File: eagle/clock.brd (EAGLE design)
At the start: 160 x 100 mm, 55 parts, among them CN1 ARDUINO_SHIELDNO_SILK, IC1 TPS55330TRE, IC2 TCS3472FN, Q1 BC817-40SMD, Q2 SUD50P04-13L

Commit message: came up with a better location for the buttons
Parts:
- moved LED0 101.0 mm to (14.0, 69.0)
- moved LED6 100.3 mm to (14.0, 57.0)
- moved LED12 99.7 mm to (14.0, 45.0)
- moved LED1 97.1 mm to (26.0, 69.0)
- moved LED7 96.3 mm to (26.0, 57.0)
- moved LED13 95.8 mm to (26.0, 45.0)
- moved LED2 93.2 mm to (38.0, 69.0)
- moved LED8 92.4 mm to (38.0, 57.0)
- moved LED14 91.8 mm to (38.0, 45.0)
- moved LED3 89.3 mm to (50.0, 69.0)
- moved LED9 88.5 mm to (50.0, 57.0)
- moved LED15 87.8 mm to (50.0, 45.0)
- moved LED4 85.4 mm to (62.0, 69.0)
- moved LED10 84.5 mm to (62.0, 57.0)
- moved LED16 83.9 mm to (62.0, 45.0)
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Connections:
- removed net N$26: CN1.A0, LEFT.P$1
- removed net N$27: CN1.A1, DOWN.P$1
- removed net N$28: CN1.A2, UP.P$1
- removed net N$29: CN1.A3, RIGHT.P$1
- new net N$1: CN1.A3, LEFT.P$1
- new net N$2: CN1.A2, DOWN.P$1
- new net N$3: CN1.A1, UP.P$1
- new net N$4: CN1.A0, RIGHT.P$1

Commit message: Almost finished layout
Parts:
- added C19: 10uF, rcl:C1206K
- added R9: 1k, rcl:R0603
- moved R5 105.6 mm to (64.8, 5.08), flipped to the bottom
- moved Q1 101.1 mm to (70.5, 3.17), flipped to the bottom, turned to 180 degrees
- moved R6 89.9 mm to (73.7, 5.08), flipped to the bottom, turned to 270 degrees
- moved Q2 89.9 mm to (80.6, 5.08), flipped to the bottom, turned to 90 degrees
- moved R7 84.9 mm to (16.5, 48.9), turned to 0 degrees
- moved R8 82.5 mm to (16.5, 50.8), turned to 0 degrees
- moved IC2 81.5 mm to (18.2, 50.8), turned to 270 degrees
- moved C10 80.2 mm to (16.5, 52.7), turned to 0 degrees
- moved C18 79.9 mm to (14.0, 46.4)
- moved C7 75.5 mm to (81.9, 34.9), flipped to the bottom, turned to 180 degrees
- moved C8 72.1 mm to (81.9, 37.5), flipped to the bottom, turned to 180 degrees
- moved D1 70.5 mm to (76.2, 38.7), flipped to the bottom, turned to 90 degrees
- moved L1 70.5 mm to (67.3, 38.7), flipped to the bottom, turned to 180 degrees
- moved C13 70.5 mm to (64.8, 15.9), turned to 90 degrees
- moved C9 69.0 mm to (81.9, 40.0), flipped to the bottom, turned to 180 degrees
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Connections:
- new net N$6: CN1.TX, R9.1
- net GND: now also C19.2
- net LIGHT-INT: now also R9.2; no longer CN1.D7
- net PWR-EN: now also CN1.A5; no longer CN1.D9
- net SMPSU-OUTPUT: now also C19.1
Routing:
- net 3.3V: track 9.12 -> 282.4 mm, vias 1 -> 19
- net 5V: track 0.00 -> 271.1 mm, vias 0 -> 24
- net N$25: track 0.00 -> 80.0 mm, vias 0 -> 2
- net N$19: track 0.00 -> 77.3 mm
- net LED-DATA: track 0.00 -> 75.9 mm
- net N$6: track 0.00 -> 74.4 mm, vias 0 -> 1
- net SCL: track 2.36 -> 76.3 mm
- net SDA: track 3.16 -> 68.6 mm
- net SMPSU-OUTPUT: track 16.5 -> 67.8 mm
- net PWR-EN: track 0.00 -> 50.0 mm
- net N$4: track 0.00 -> 43.9 mm
- net SW: track 0.00 -> 31.2 mm
- net N$3: track 0.00 -> 28.6 mm
- net LED-PWM: track 0.00 -> 26.9 mm
- net N$1: track 0.00 -> 18.9 mm
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- added copper zone on layer 1, net GND
- added copper zone on layer 16, net GND
- removed copper zone on layer 1, net SMPSU-OUTPUT
- removed copper zone on layer 1, net SW
- removed copper zone on layer 1, net V_BATT
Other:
- board size 160 x 100 mm -> 78.7 x 78.7 mm

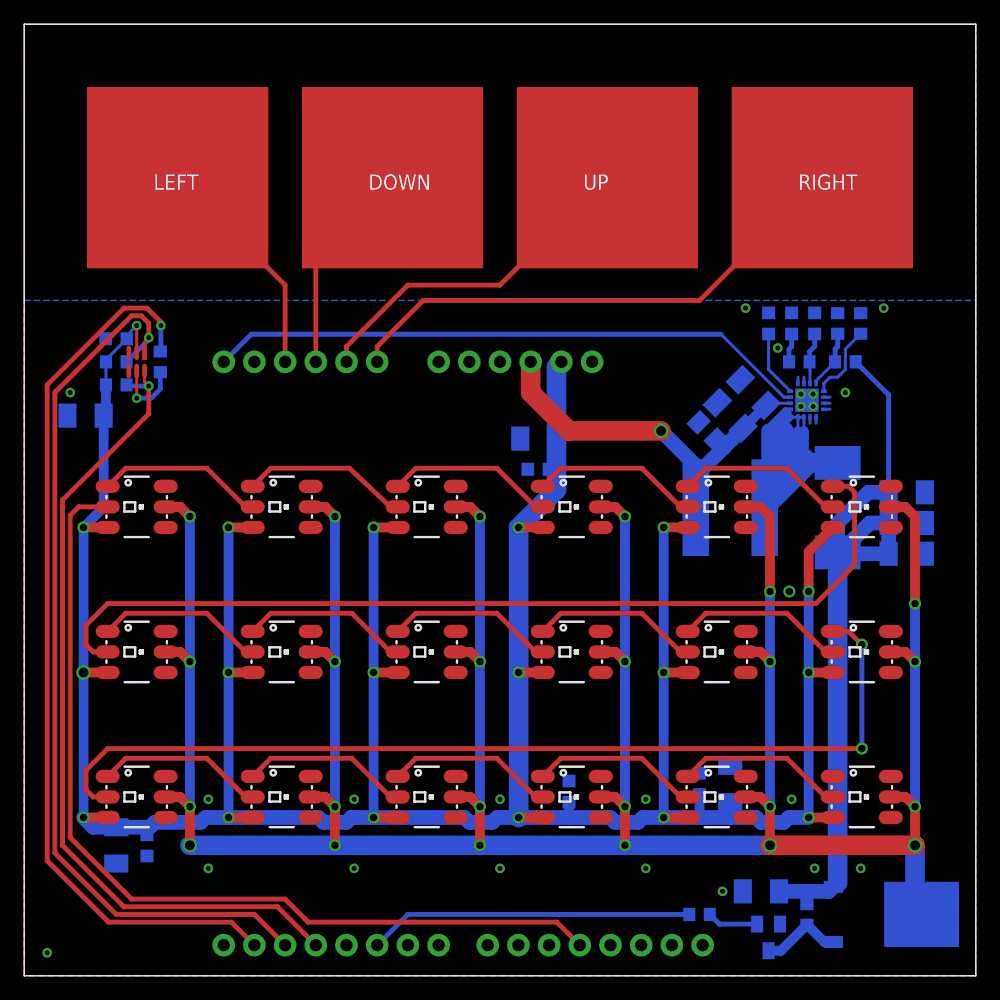
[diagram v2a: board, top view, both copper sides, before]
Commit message: Seems like there's a bug with the polyfills in eagle. I gave up and I just used one back plane
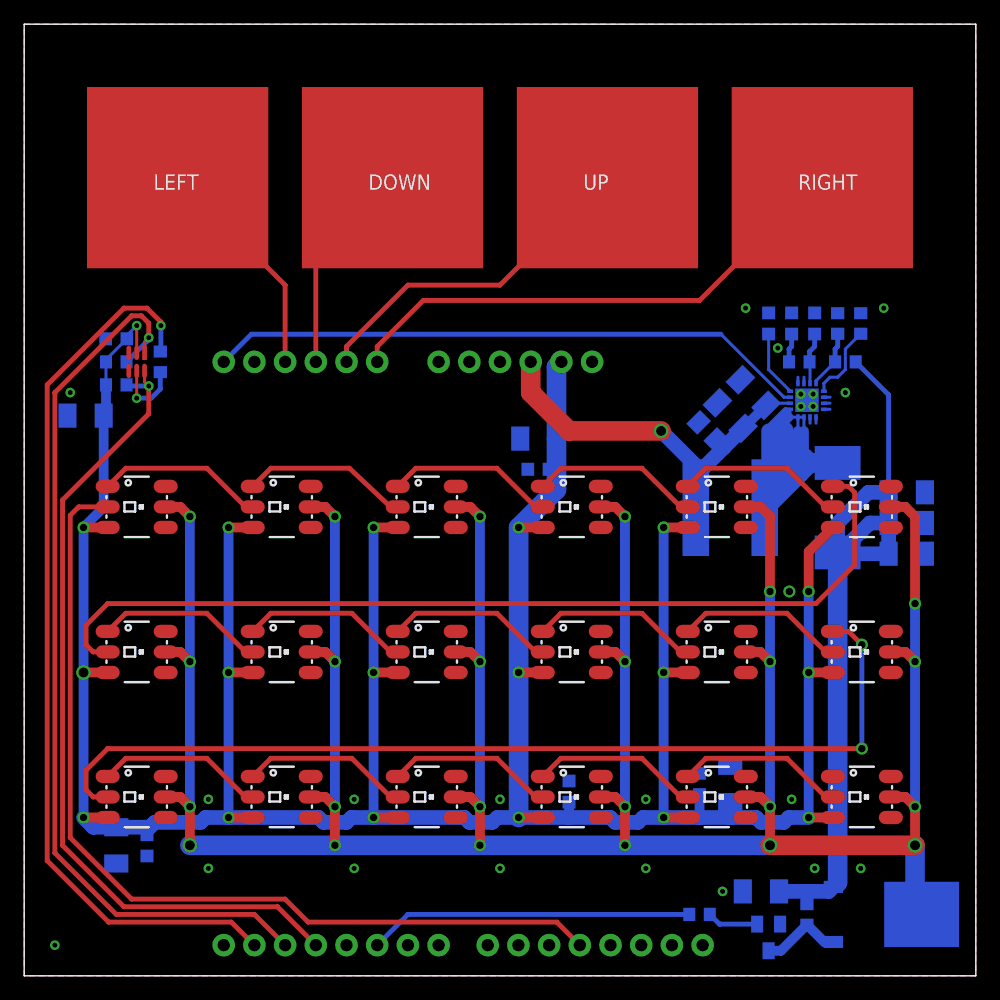
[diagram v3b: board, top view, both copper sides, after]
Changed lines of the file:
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@@
 <grid distance="25" unitdist="mil" unit="mil" style="dots" multiple="1" display="yes" altdistance="0.025" altunitdist="inch" altunit="inch"/>
 <layers>
-<layer number="1" name="Top" color="4" fill="1" visible="yes" active="yes"/>
+<layer number="1" name="Top" color="4" fill="1" visible="no" active="yes"/>
 <layer number="2" name="Route2" color="1" fill="3" visible="no" active="no"/>
 <layer number="3" name="Route3" color="4" fill="3" visible="no" active="no"/>
@@
 <contactref element="LED17" pad="6"/>
 <contactref element="C19" pad="2"/>
-<polygon width="0.254" layer="16" isolate="0.254">
-<vertex x="8.89" y="55.88"/>
-<vertex x="87.63" y="55.88"/>
+<polygon width="0.254" layer="16" pour="hatch" isolate="0.254">
+<vertex x="8.89" y="78.74"/>
+<vertex x="87.63" y="78.74"/>
 <vertex x="87.63" y="0"/>
 <vertex x="8.89" y="0"/>
@@
 <via x="36.195" y="8.89" extent="1-16" drill="0.4064" diameter="0.4064" shape="octagon"/>
 <via x="24.13" y="8.89" extent="1-16" drill="0.4064" diameter="0.4064" shape="octagon"/>
-<via x="10.795" y="1.905" extent="1-16" drill="0.4064" diameter="0.4064" shape="octagon"/>
-<polygon width="0.4064" layer="16" pour="hatch" isolate="0.3048">
-<vertex x="8.89" y="55.88"/>
-<vertex x="87.63" y="55.88"/>
-<vertex x="87.63" y="78.74"/>
-<vertex x="8.89" y="78.74"/>
-</polygon>
+<via x="11.43" y="2.54" extent="1-16" drill="0.4064" diameter="0.4064" shape="octagon"/>
+<wire x1="74.41" y1="46.225" x2="73.91" y2="46.225" width="0" layer="19" extent="16-16"/>
+<wire x1="73.41" y1="49.025" x2="72.91" y2="49.025" width="0" layer="19" extent="16-16"/>
 </signal>
 <signal name="SW">

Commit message: Finished silk screen touches. Ready to order.
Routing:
- net GND: track 3.53 -> 4.53 mm, vias 23 -> 24
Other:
- board text added: "Alexandru Stan - Fall 2013"
- board text added: "Binary Clock v2.0"
- board text added: "HyperTriangle"

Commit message: Ready to order
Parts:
- moved DOWN 1.91 mm to (39.4, 64.1)
- moved LEFT 1.91 mm to (21.6, 64.1)
- moved RIGHT 1.91 mm to (74.9, 64.1)
- moved UP 1.91 mm to (57.1, 64.1)
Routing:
- net N$1: track 18.9 -> 17.0 mm
- net N$2: track 17.9 -> 16.0 mm
- net N$4: track 43.9 -> 43.1 mm
- net GND: vias 24 -> 28
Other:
- board size 78.7 x 78.7 mm -> 78.7 x 76.8 mm
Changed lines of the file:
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@@
 <plain>
 <wire x1="8.89" y1="0" x2="87.63" y2="0" width="0" layer="20"/>
-<wire x1="87.63" y1="0" x2="87.63" y2="78.74" width="0" layer="20"/>
-<wire x1="87.63" y1="78.74" x2="8.89" y2="78.74" width="0" layer="20"/>
-<wire x1="8.89" y1="78.74" x2="8.89" y2="0" width="0" layer="20"/>
+<wire x1="87.63" y1="0" x2="87.63" y2="76.835" width="0" layer="20"/>
+<wire x1="87.63" y1="76.835" x2="8.89" y2="76.835" width="0" layer="20"/>
+<wire x1="8.89" y1="76.835" x2="8.89" y2="0" width="0" layer="20"/>
 <wire x1="22.86" y1="53.34" x2="76.2" y2="53.34" width="0.254" layer="48"/>
 <wire x1="76.2" y1="0" x2="76.2" y2="6.985" width="0.254" layer="48"/>
@@
 <dimension x1="87.63" y1="71.12" x2="8.89" y2="71.12" x3="48.26" y3="-7.62" textsize="1.778" layer="48" unit="mil"/>
 <polygon width="0.4064" layer="21">
-<vertex x="53.975" y="63.5"/>
-<vertex x="57.15" y="68.58"/>
-<vertex x="60.325" y="63.5"/>
+<vertex x="53.975" y="61.595"/>
+<vertex x="57.15" y="66.675"/>
+<vertex x="60.325" y="61.595"/>
 </polygon>
 <polygon width="0.4064" layer="21">
-<vertex x="42.545" y="68.58"/>
-<vertex x="39.37" y="63.5"/>
-<vertex x="36.195" y="68.58"/>
+<vertex x="42.545" y="66.675"/>
+<vertex x="39.37" y="61.595"/>
+<vertex x="36.195" y="66.675"/>
 </polygon>
 <polygon width="0.4064" layer="21">
-<vertex x="24.13" y="62.865"/>
-<vertex x="19.05" y="66.04"/>
-<vertex x="24.13" y="69.215"/>
+<vertex x="24.13" y="60.96"/>
+<vertex x="19.05" y="64.135"/>
+<vertex x="24.13" y="67.31"/>
 </polygon>
 <polygon width="0.4064" layer="21">
-<vertex x="72.39" y="69.215"/>
-<vertex x="77.47" y="66.04"/>
-<vertex x="72.39" y="62.865"/>
+<vertex x="72.39" y="67.31"/>
+<vertex x="77.47" y="64.135"/>
+<vertex x="72.39" y="60.96"/>
 </polygon>
-<wire x1="74.93" y1="57.15" x2="71.12" y2="50.4825" width="0.4064" layer="25"/>
-<wire x1="71.12" y1="50.4825" x2="78.74" y2="50.4825" width="0.4064" layer="25"/>
-<wire x1="78.74" y1="50.4825" x2="74.93" y2="57.15" width="0.4064" layer="25"/>
-<wire x1="71.12" y1="50.4825" x2="76.5175" y2="52.3875" width="0.4064" layer="25"/>
-<wire x1="74.4855" y1="54.4195" x2="78.74" y2="50.4825" width="0.4064" layer="25"/>
-<wire x1="74.93" y1="57.15" x2="73.9775" y2="51.562" width="0.4064" layer="25"/>
-<text x="68.58" y="47.625" size="1.27" layer="25" font="vector">HyperTriangle</text>
-<text x="68.58" y="45.72" size="1.016" layer="21" font="vector">Binary Clock v2.0</text>
-<text x="68.58" y="44.45" size="0.635" layer="21" font="vector">Alexandru Stan - Fall 2013</text>
+<wire x1="75.565" y1="55.445" x2="71.755" y2="48.7775" width="0.4064" layer="25"/>
+<wire x1="71.755" y1="48.7775" x2="79.375" y2="48.7775" width="0.4064" layer="25"/>
+<wire x1="79.375" y1="48.7775" x2="75.565" y2="55.445" width="0.4064" layer="25"/>
+<wire x1="71.755" y1="48.7775" x2="77.1525" y2="50.6825" width="0.4064" layer="25"/>
+<wire x1="75.1205" y1="52.7145" x2="79.375" y2="48.7775" width="0.4064" layer="25"/>
+<wire x1="75.565" y1="55.445" x2="74.6125" y2="49.857" width="0.4064" layer="25"/>
+<text x="69.215" y="45.92" size="1.27" layer="25" font="vector">HyperTriangle</text>
+<text x="69.215" y="44.015" size="1.016" layer="21" font="vector">Binary Clock v2.0</text>
+<text x="69.215" y="42.745" size="0.635" layer="21" font="vector">Alexandru Stan - Fall 2013</text>
 </plain>
 <attributes>
@@
 </element>
 <element name="C15" library="rcl" package="C0603K" value="100nF" x="19.05" y="10.795" smashed="yes" rot="MR270">
-<attribute name="NAME" x="19.67" y="7.785" size="1.27" layer="26" rot="MR270"/>
+<attribute name="NAME" x="19.67" y="7.985" size="1.27" layer="26" rot="MR270"/>
 </element>
 <element name="C16" library="rcl" package="C1206K" value="10uF" x="16.51" y="10.795" smashed="yes" rot="MR270">
@@
 </element>
 <element name="CN1" library="SparkFun-Boards" package="DUEMILANOVE_VIAS" value="ARDUINO_SHIELDNO_SILK" x="67.31" y="0" rot="R90"/>
-<element name="LEFT" library="HyperTriangle" package="CAP-PAD-15MM" value="CAP-PAD15MM" x="21.59" y="66.04" smashed="yes">
-<attribute name="NAME" x="14.51" y="59.325" size="1.27" layer="51"/>
-</element>
-<element name="DOWN" library="HyperTriangle" package="CAP-PAD-15MM" value="CAP-PAD15MM" x="39.37" y="66.04" smashed="yes">
-<attribute name="NAME" x="32.29" y="59.325" size="1.27" layer="51"/>
-</element>
-<element name="UP" library="HyperTriangle" package="CAP-PAD-15MM" value="CAP-PAD15MM" x="57.15" y="66.04" smashed="yes">
-<attribute name="NAME" x="50.07" y="59.325" size="1.27" layer="51"/>
-</element>
-<element name="RIGHT" library="HyperTriangle" package="CAP-PAD-15MM" value="CAP-PAD15MM" x="74.93" y="66.04" smashed="yes">
-<attribute name="NAME" x="67.85" y="59.325" size="1.27" layer="51"/>
+<element name="LEFT" library="HyperTriangle" package="CAP-PAD-15MM" value="CAP-PAD15MM" x="21.59" y="64.135" smashed="yes">
+<attribute name="NAME" x="14.51" y="57.42" size="1.27" layer="51"/>
+</element>
+<element name="DOWN" library="HyperTriangle" package="CAP-PAD-15MM" value="CAP-PAD15MM" x="39.37" y="64.135" smashed="yes">
+<attribute name="NAME" x="32.29" y="57.42" size="1.27" layer="51"/>
+</element>
+<element name="UP" library="HyperTriangle" package="CAP-PAD-15MM" value="CAP-PAD15MM" x="57.15" y="64.135" smashed="yes">
+<attribute name="NAME" x="50.07" y="57.42" size="1.27" layer="51"/>
+</element>
+<element name="RIGHT" library="HyperTriangle" package="CAP-PAD-15MM" value="CAP-PAD15MM" x="74.93" y="64.135" smashed="yes">
+<attribute name="NAME" x="67.85" y="57.42" size="1.27" layer="51"/>
 </element>
 <element name="LED0" library="HyperTriangle" package="LED-TRICOLOR-5050-IC" value="WS2812" x="18.2" y="38.8" smashed="yes"/>
@@
 <element name="LED17" library="HyperTriangle" package="LED-TRICOLOR-5050-IC" value="WS2812" x="78.2" y="14.8" smashed="yes"/>
 <element name="C19" library="rcl" package="C1206K" value="10uF" x="69.85" y="6.985" smashed="yes" rot="MR0">
-<attribute name="NAME" x="70.815" y="8.72" size="1.016" layer="26" rot="MR0"/>
+<attribute name="NAME" x="70.815" y="8.72" size="1.27" layer="26" rot="MR0"/>
 </element>
 <element name="R9" library="rcl" package="R0603" value="1k" x="20.155" y="50.8" smashed="yes" rot="MR270">
@@
 <contactref element="C19" pad="2"/>
 <polygon width="0.254" layer="16" pour="hatch" isolate="0.254">
-<vertex x="8.89" y="78.74"/>
-<vertex x="87.63" y="78.74"/>
+<vertex x="8.89" y="76.835"/>
+<vertex x="87.63" y="76.835"/>
 <vertex x="87.63" y="0"/>
 <vertex x="8.89" y="0"/>
 </polygon>
 <polygon width="0.254" layer="1" isolate="0.254">
-<vertex x="8.89" y="78.74"/>
-<vertex x="87.63" y="78.74"/>
+<vertex x="8.89" y="76.835"/>
+<vertex x="87.63" y="76.835"/>
 <vertex x="87.63" y="0"/>
 <vertex x="8.89" y="0"/>
@@
 <wire x1="73.91" y1="46.225" x2="74.41" y2="46.225" width="0.254" layer="16"/>
 <wire x1="72.91" y1="49.025" x2="73.41" y2="49.025" width="0.254" layer="16"/>
+<via x="49.53" y="54.61" extent="1-16" drill="0.4064" diameter="0.4064" shape="octagon"/>
+<via x="34.29" y="54.61" extent="1-16" drill="0.4064" diameter="0.4064" shape="octagon"/>
+<via x="31.75" y="54.61" extent="1-16" drill="0.4064" diameter="0.4064" shape="octagon"/>
+<via x="29.21" y="54.61" extent="1-16" drill="0.4064" diameter="0.4064" shape="octagon"/>
 <wire x1="73.152" y1="47.117" x2="73.66" y2="47.625" width="0" layer="19" extent="16-16"/>
 </signal>
@@
 <contactref element="CN1" pad="A3"/>
 <contactref element="LEFT" pad="P$1"/>
-<wire x1="30.48" y1="50.8" x2="30.48" y2="57.15" width="0.4064" layer="1"/>
-<wire x1="30.48" y1="57.15" x2="21.59" y2="66.04" width="0.4064" layer="1"/>
+<wire x1="30.48" y1="50.8" x2="30.48" y2="55.245" width="0.4064" layer="1"/>
+<wire x1="30.48" y1="55.245" x2="21.59" y2="64.135" width="0.4064" layer="1"/>
 </signal>
 <signal name="N$2">
 <contactref element="CN1" pad="A2"/>
 <contactref element="DOWN" pad="P$1"/>
-<wire x1="33.02" y1="50.8" x2="33.02" y2="59.69" width="0.4064" layer="1"/>
-<wire x1="33.02" y1="59.69" x2="39.37" y2="66.04" width="0.4064" layer="1"/>
+<wire x1="33.02" y1="50.8" x2="33.02" y2="57.785" width="0.4064" layer="1"/>
+<wire x1="33.02" y1="57.785" x2="39.37" y2="64.135" width="0.4064" layer="1"/>
 </signal>
 <signal name="N$3">
 <contactref element="CN1" pad="A1"/>
 <contactref element="UP" pad="P$1"/>
-<wire x1="35.56" y1="50.8" x2="35.56" y2="52.07" width="0.4064" layer="1"/>
-<wire x1="35.56" y1="52.07" x2="40.64" y2="57.15" width="0.4064" layer="1"/>
-<wire x1="40.64" y1="57.15" x2="48.26" y2="57.15" width="0.4064" layer="1"/>
-<wire x1="48.26" y1="57.15" x2="57.15" y2="66.04" width="0.4064" layer="1"/>
+<wire x1="38.1" y1="55.245" x2="48.26" y2="55.245" width="0.4064" layer="1"/>
+<wire x1="48.26" y1="55.245" x2="57.15" y2="64.135" width="0.4064" layer="1"/>
+<wire x1="38.1" y1="55.245" x2="35.56" y2="52.705" width="0.4064" layer="1"/>
+<wire x1="35.56" y1="52.705" x2="35.56" y2="50.8" width="0.4064" layer="1"/>
 </signal>
 <signal name="N$4">
 <contactref element="CN1" pad="A0"/>
 <contactref element="RIGHT" pad="P$1"/>
-<wire x1="38.1" y1="50.8" x2="38.1" y2="52.07" width="0.4064" layer="1"/>
-<wire x1="38.1" y1="52.07" x2="41.91" y2="55.88" width="0.4064" layer="1"/>
-<wire x1="41.91" y1="55.88" x2="64.77" y2="55.88" width="0.4064" layer="1"/>
-<wire x1="64.77" y1="55.88" x2="74.93" y2="66.04" width="0.4064" layer="1"/>
+<wire x1="39.37" y1="53.34" x2="64.135" y2="53.34" width="0.4064" layer="1"/>
+<wire x1="64.135" y1="53.34" x2="74.93" y2="64.135" width="0.4064" layer="1"/>
+<wire x1="39.37" y1="53.34" x2="38.1" y2="52.07" width="0.4064" layer="1"/>
+<wire x1="38.1" y1="52.07" x2="38.1" y2="50.8" width="0.4064" layer="1"/>
 </signal>
 <signal name="N$6">
